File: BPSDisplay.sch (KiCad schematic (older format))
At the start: 27 parts, among them J1 SWD, J6 CAN_LogicAnalyzer, J7 SPI0_LogicAnalyzer, J8 GEN_LogicAnalyzer, J9 USART_LogicAnalyzer, P1 Conn_02x20_Odd_Even, SW1 Reset, U1 STM32F413RHTx, Y1 8M

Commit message: Adds LED for supplementals, deletes unncessary files, and links all symbols to the submodule
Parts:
- added D2: PowerOn, LED_SMD:LED_0805_2012Metric, symbol Device:LED_ALT
- added R4: 750, Resistor_SMD:R_0805_2012Metric, symbol Device:R
- LOGO1: value Logo_Placeholder -> UTSVT
- LOGO2: value Logo_Placeholder -> Dr. Hallock
- MK1, MK2, MK3, MK4, MK5: symbol BPSDisplay-rescue:Mounting_Hole-Mechanical-BPSDisplay-rescue -> Mechanical:MountingHole
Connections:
- wire segments 165 -> 169
- no-connect marks 48 -> 47
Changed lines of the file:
@@
 ID_SD and ID_SC PINS:\nThese pins are reserved for HAT ID EEPROM.\n\nAt boot time this I2C interface will be\ninterrogated to look for an EEPROM\nthat identifes the attached board and\nallows automagic setup of the GPIOs\n(and optionally, Linux drivers).\n\nDO NOT USE these pins for anything other\nthan attaching an I2C ID EEPROM. Leave\nunconnected if ID EEPROM not required.
 $Comp
-L BPSDisplay-rescue:Mounting_Hole-Mechanical-BPSDisplay-rescue MK1
+L Mechanical:MountingHole MK1
 U 1 1 5834FB2E
 P 3000 7200
@@
 $EndComp
 $Comp
-L BPSDisplay-rescue:Mounting_Hole-Mechanical-BPSDisplay-rescue MK2
+L Mechanical:MountingHole MK2
 U 1 1 5834FBEF
 P 3450 7200
@@
 $EndComp
 $Comp
-L BPSDisplay-rescue:Mounting_Hole-Mechanical-BPSDisplay-rescue MK4
+L Mechanical:MountingHole MK4
 U 1 1 5834FC19
 P 3000 7400
@@
 Text Label 4850 4000 0    50   ~ 0
 USART6_RX
-$Comp
-L power:GND #PWR025
-U 1 1 5D764CDB
-P 2000 6250
-F 0 "#PWR025" H 2000 6000 50  0001 C CNN
-F 1 "GND" H 2000 6100 50  0000 C CNN
-F 2 "" H 2000 6250 50  0000 C CNN
-F 3 "" H 2000 6250 50  0000 C CNN
-	1    2000 6250
-	1    0    0    -1
-$EndComp
-Wire Wire Line
-	2000 6250 2000 6150
-Wire Wire Line
-	2000 6150 1900 6150
-Wire Wire Line
-	1900 6050 2250 6050
-Wire Wire Line
-	2250 6050 2250 5850
-$Comp
-L power:+3.3V #PWR024
-U 1 1 5D771241
-P 2250 5850
-F 0 "#PWR024" H 2250 5700 50  0001 C CNN
-F 1 "+3.3V" H 2250 5990 50  0000 C CNN
-F 2 "" H 2250 5850 50  0000 C CNN
-F 3 "" H 2250 5850 50  0000 C CNN
-	1    2250 5850
-	1    0    0    -1
-$EndComp
-Wire Wire Line
-	2000 5950 2000 5850
-$Comp
-L power:+5V #PWR023
-U 1 1 5D77123B
-P 2000 5850
-F 0 "#PWR023" H 2000 5700 50  0001 C CNN
-F 1 "+5V" H 2000 5990 50  0000 C CNN
-F 2 "" H 2000 5850 50  0000 C CNN
-F 3 "" H 2000 5850 50  0000 C CNN
-	1    2000 5850
-	1    0    0    -1
-$EndComp
-Wire Wire Line
-	1900 5950 2000 5950
-$Sheet
-S 1150 5850 750  400
-U 5D76E7C8
-F0 "Power Dist" 50
-F1 "PowerDist.sch" 50
-F2 "GND" O R 1900 6150 50
-F3 "+3.3V" O R 1900 6050 50
-F4 "+5V" O R 1900 5950 50
-$EndSheet
 NoConn ~ 6750 1700
 NoConn ~ 6750 1800
@@
 NoConn ~ 5350 3500
 $Comp
-L BPSDisplay-rescue:Mounting_Hole-Mechanical-BPSDisplay-rescue MK3
+L Mechanical:MountingHole MK3
 U 1 1 5D979DD2
 P 4650 7200
@@
 $EndComp
 $Comp
-L BPSDisplay-rescue:Mounting_Hole-Mechanical-BPSDisplay-rescue MK5
+L Mechanical:MountingHole MK5
 U 1 1 5D97A2E5
 P 4650 7400
@@
 	9800 1400 9800 1350
 NoConn ~ 5350 4300
-NoConn ~ 5350 4400
 NoConn ~ 5350 4500
 Wire Wire Line
@@
 GPIO8(SPI0_CE_N)
 $Comp
-L BPSDisplay:GND #PWR020
+L power:GND #PWR020
 U 1 1 5F8C3D7F
 P 9400 4150
@@
 $EndComp
 $Comp
-L BPSDisplay:GND #PWR022
+L power:GND #PWR022
 U 1 1 5F91429A
 P 9450 5000
@@
 $EndComp
 $Comp
-L BPSDisplay:GND #PWR029
+L power:GND #PWR029
 U 1 1 5F937BE0
 P 9450 5750
@@
 P 5500 7150
 F 0 "LOGO1" H 5500 7300 50  0001 C CNN
-F 1 "Logo_Placeholder" H 5640 7150 50  0000 L CNN
+F 1 "UTSVT" H 5640 7150 50  0000 L CNN
 F 2 "UTSVT_Special:UTSVT_Logo_Symbol" H 5500 7225 50  0001 C CNN
 F 3 "" H 5500 7225 50  0001 C CNN
@@
 P 5500 6800
 F 0 "LOGO2" H 5500 6950 50  0001 C CNN
-F 1 "Logo_Placeholder" H 5640 6800 50  0000 L CNN
+F 1 "Dr. Hallock" H 5640 6800 50  0000 L CNN
 F 2 "UTSVT_Special:Hallock_Image_Tiny" H 5500 6875 50  0001 C CNN
 F 3 "" H 5500 6875 50  0001 C CNN
@@
 	1    0    0    -1
 $EndComp
+$Sheet
+S 1100 4950 750  400
+U 5D76E7C8
+F0 "Power Dist" 50
+F1 "PowerDist.sch" 50
+F2 "GND" O R 1850 5250 50
+F3 "+3.3V" O R 1850 5150 50
+F4 "+5V" O R 1850 5050 50
+$EndSheet
+Wire Wire Line
+	1850 5050 1950 5050
+$Comp
+L power:+5V #PWR023
+U 1 1 5D77123B
+P 1950 4950
+F 0 "#PWR023" H 1950 4800 50  0001 C CNN
+F 1 "+5V" H 1950 5090 50  0000 C CNN
+F 2 "" H 1950 4950 50  0000 C CNN
+F 3 "" H 1950 4950 50  0000 C CNN
+	1    1950 4950
+	1    0    0    -1
+$EndComp
+Wire Wire Line
+	1950 5050 1950 4950
+$Comp
+L power:+3.3V #PWR024
+U 1 1 5D771241
+P 2200 4950
+F 0 "#PWR024" H 2200 4800 50  0001 C CNN
+F 1 "+3.3V" H 2200 5090 50  0000 C CNN
+F 2 "" H 2200 4950 50  0000 C CNN
+F 3 "" H 2200 4950 50  0000 C CNN
+	1    2200 4950
+	1    0    0    -1
+$EndComp
+Wire Wire Line
+	2200 5150 2200 4950
+Wire Wire Line
+	1850 5150 2200 5150
+Wire Wire Line
+	1950 5250 1850 5250
+Wire Wire Line
+	1950 5350 1950 5250
+$Comp
+L power:GND #PWR025
+U 1 1 5D764CDB
+P 1950 5350
+F 0 "#PWR025" H 1950 5100 50  0001 C CNN
+F 1 "GND" H 1950 5200 50  0000 C CNN
+F 2 "" H 1950 5350 50  0000 C CNN
+F 3 "" H 1950 5350 50  0000 C CNN
+	1    1950 5350
+	1    0    0    -1
+$EndComp
+$Comp
+L Device:LED_ALT D?
+U 1 1 5FDE8C5D
+P 4250 4200
+AR Path="/5D76E7C8/5FDE8C5D" Ref="D?"  Part="1"
+AR Path="/5FDE8C5D" Ref="D2"  Part="1"
+F 0 "D2" V 4288 4082 50  0000 R CNN
+F 1 "PowerOn" V 4197 4082 50  0000 R CNN
+F 2 "LED_SMD:LED_0805_2012Metric" H 4250 4200 50  0001 C CNN
+F 3 "~" H 4250 4200 50  0001 C CNN
+F 4 "Red" V 4250 4200 50  0001 C CNN "Color"
+F 5 "" V 4250 4200 50  0001 C CNN "P/N"
+	1    4250 4200
+	0    -1   -1   0
+$EndComp
+$Comp
+L Device:R R?
+U 1 1 5FDE8C63
+P 4250 3850
+AR Path="/5D76E7C8/5FDE8C63" Ref="R?"  Part="1"
+AR Path="/5FDE8C63" Ref="R4"  Part="1"
+F 0 "R4" H 4320 3896 50  0000 L CNN
+F 1 "750" H 4320 3805 50  0000 L CNN
+F 2 "Resistor_SMD:R_0805_2012Metric" V 4180 3850 50  0001 C CNN
+F 3 "~" H 4250 3850 50  0001 C CNN
+	1    4250 3850
+	1    0    0    -1
+$EndComp
+Wire Wire Line
+	4250 4050 4250 4000
+Wire Wire Line
+	5350 4400 4250 4400
+Wire Wire Line
+	4250 4350 4250 4400
+Wire Wire Line
+	4250 3700 4250 3650
+$Comp
+L power:+3.3V #PWR0101
+U 1 1 5FE10F92
+P 4250 3650
+F 0 "#PWR0101" H 4250 3500 50  0001 C CNN
+F 1 "+3.3V" H 4250 3790 50  0000 C CNN
+F 2 "" H 4250 3650 50  0000 C CNN
+F 3 "" H 4250 3650 50  0000 C CNN
+	1    4250 3650
+	1    0    0    -1
+$EndComp

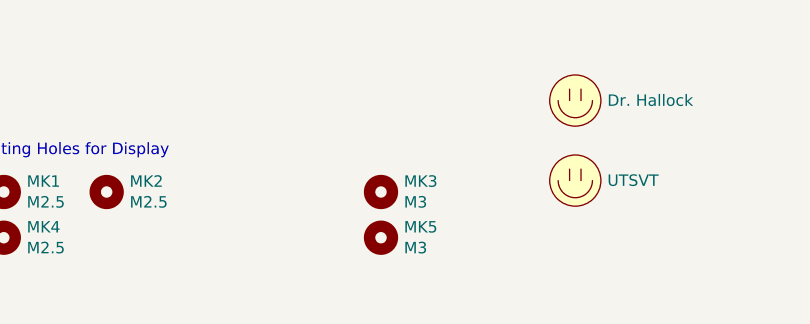
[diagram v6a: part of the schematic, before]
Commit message: Redo most of the layout to fix issues.
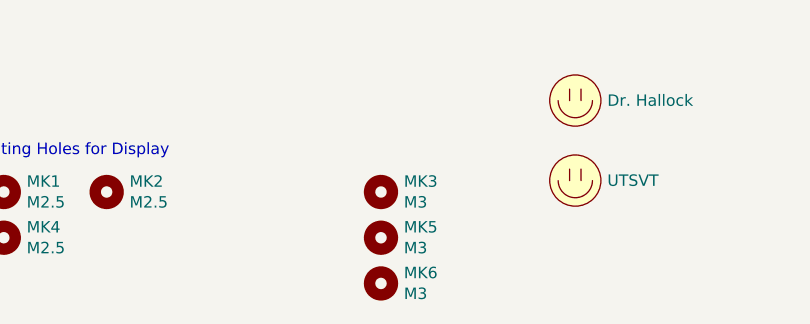
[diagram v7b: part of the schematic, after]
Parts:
- added MK6: M3, MountingHole:MountingHole_3mm, symbol Mechanical:MountingHole
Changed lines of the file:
@@
+	1    0    0    -1
+$EndComp
+$Comp
+L Mechanical:MountingHole MK6
+U 1 1 60697865
+P 4650 7600
+F 0 "MK6" H 4750 7646 50  0000 L CNN
+F 1 "M3" H 4750 7555 50  0000 L CNN
+F 2 "MountingHole:MountingHole_3mm" H 4650 7600 50  0001 C CNN
+F 3 "" H 4650 7600 50  0001 C CNN
+	1    4650 7600
 	1    0    0    -1
 $EndComp

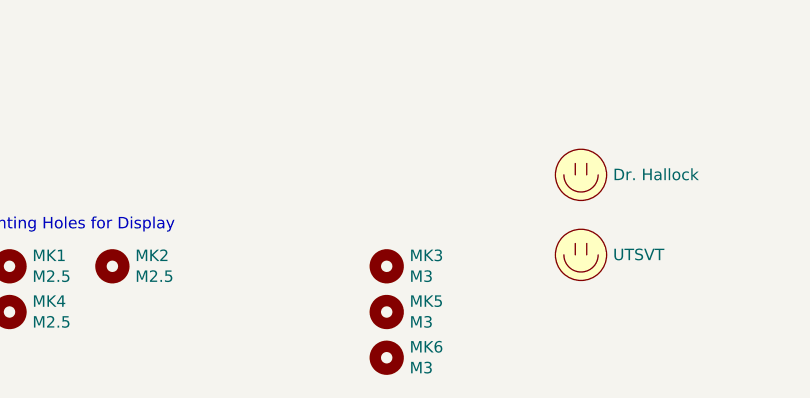
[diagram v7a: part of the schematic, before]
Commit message: Adds another mounting hole, moves PWR LED, and adds labels to test points
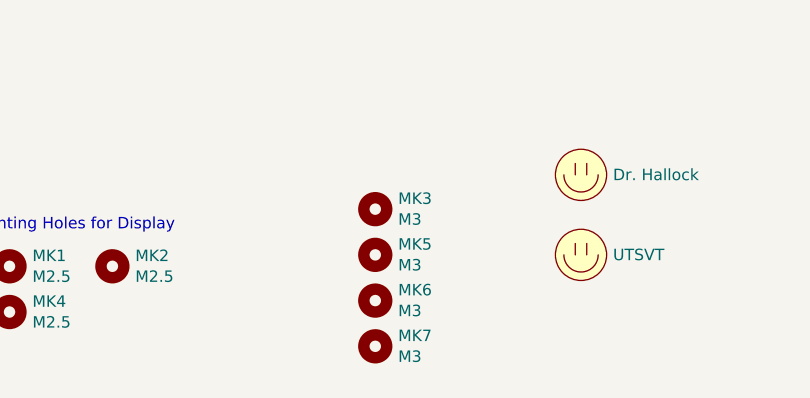
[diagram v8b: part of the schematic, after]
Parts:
- added MK7: M3, MountingHole:MountingHole_3mm, symbol Mechanical:MountingHole
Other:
- moved on the sheet: MK3, MK5, MK6
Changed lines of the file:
@@
 L Mechanical:MountingHole MK3
 U 1 1 5D979DD2
-P 4650 7200
-F 0 "MK3" H 4750 7246 50  0000 L CNN
-F 1 "M3" H 4750 7155 50  0000 L CNN
-F 2 "MountingHole:MountingHole_3mm" H 4650 7200 50  0001 C CNN
-F 3 "" H 4650 7200 50  0001 C CNN
-	1    4650 7200
+P 4600 6950
+F 0 "MK3" H 4700 6996 50  0000 L CNN
+F 1 "M3" H 4700 6905 50  0000 L CNN
+F 2 "MountingHole:MountingHole_3mm" H 4600 6950 50  0001 C CNN
+F 3 "" H 4600 6950 50  0001 C CNN
+	1    4600 6950
 	1    0    0    -1
 $EndComp
@@
 L Mechanical:MountingHole MK5
 U 1 1 5D97A2E5
-P 4650 7400
-F 0 "MK5" H 4750 7446 50  0000 L CNN
-F 1 "M3" H 4750 7355 50  0000 L CNN
-F 2 "MountingHole:MountingHole_3mm" H 4650 7400 50  0001 C CNN
-F 3 "" H 4650 7400 50  0001 C CNN
-	1    4650 7400
+P 4600 7150
+F 0 "MK5" H 4700 7196 50  0000 L CNN
+F 1 "M3" H 4700 7105 50  0000 L CNN
+F 2 "MountingHole:MountingHole_3mm" H 4600 7150 50  0001 C CNN
+F 3 "" H 4600 7150 50  0001 C CNN
+	1    4600 7150
 	1    0    0    -1
 $EndComp
@@
 L Mechanical:MountingHole MK6
 U 1 1 60697865
-P 4650 7600
-F 0 "MK6" H 4750 7646 50  0000 L CNN
-F 1 "M3" H 4750 7555 50  0000 L CNN
-F 2 "MountingHole:MountingHole_3mm" H 4650 7600 50  0001 C CNN
-F 3 "" H 4650 7600 50  0001 C CNN
-	1    4650 7600
-	1    0    0    -1
-$EndComp
+P 4600 7350
+F 0 "MK6" H 4700 7396 50  0000 L CNN
+F 1 "M3" H 4700 7305 50  0000 L CNN
+F 2 "MountingHole:MountingHole_3mm" H 4600 7350 50  0001 C CNN
+F 3 "" H 4600 7350 50  0001 C CNN
+	1    4600 7350
+	1    0    0    -1
+$EndComp
+$Comp
+L Mechanical:MountingHole MK7
+U 1 1 5FDF38F4
+P 4600 7550
+F 0 "MK7" H 4700 7596 50  0000 L CNN
+F 1 "M3" H 4700 7505 50  0000 L CNN
+F 2 "MountingHole:MountingHole_3mm" H 4600 7550 50  0001 C CNN
+F 3 "" H 4600 7550 50  0001 C CNN
+	1    4600 7550
+	1    0    0    -1
+$EndComp
